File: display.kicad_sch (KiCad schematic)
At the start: 1 part, among them U1 AM6254ATCGHAALW

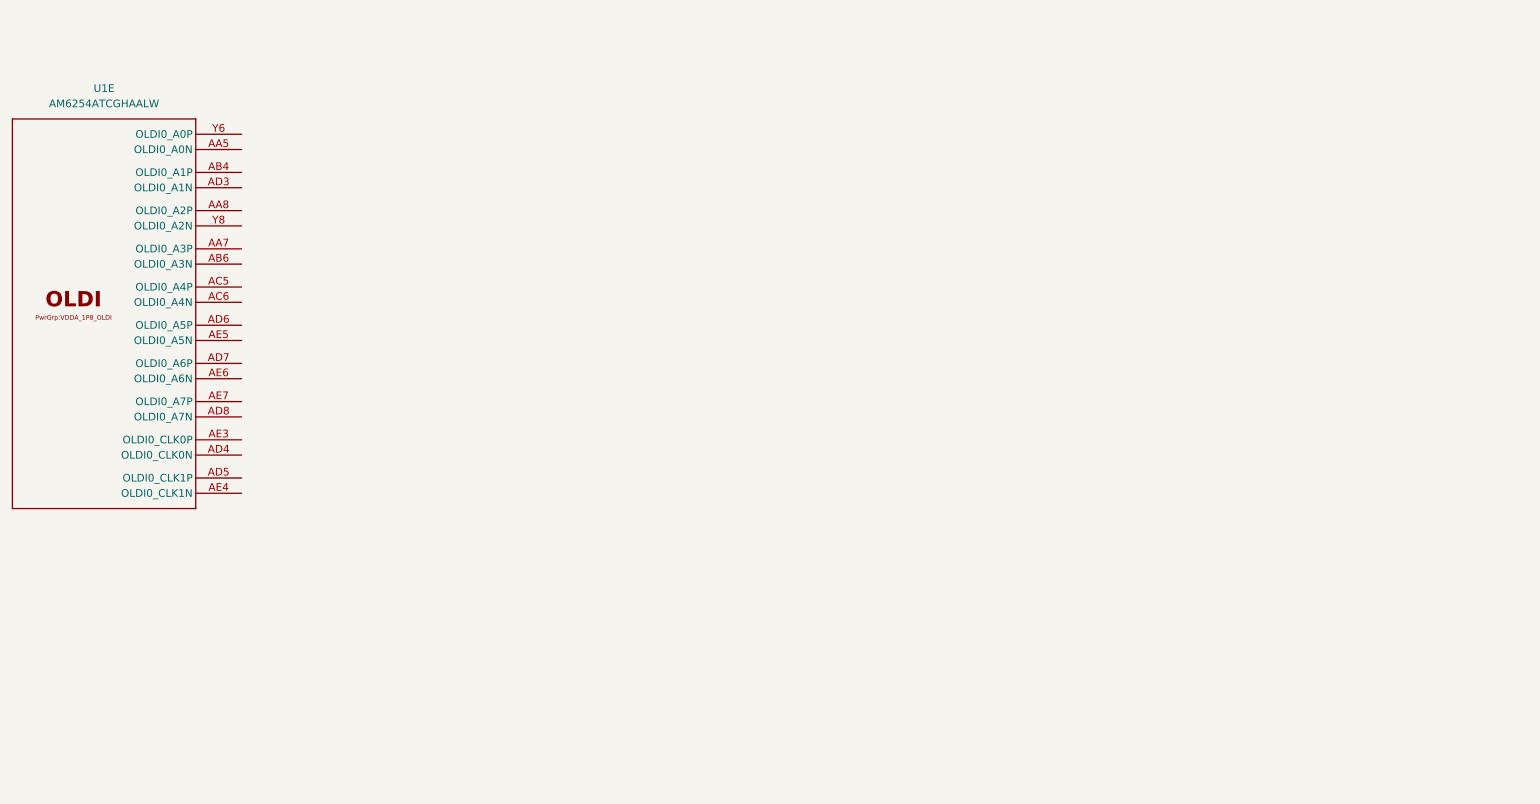
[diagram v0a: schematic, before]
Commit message: Display draft connections
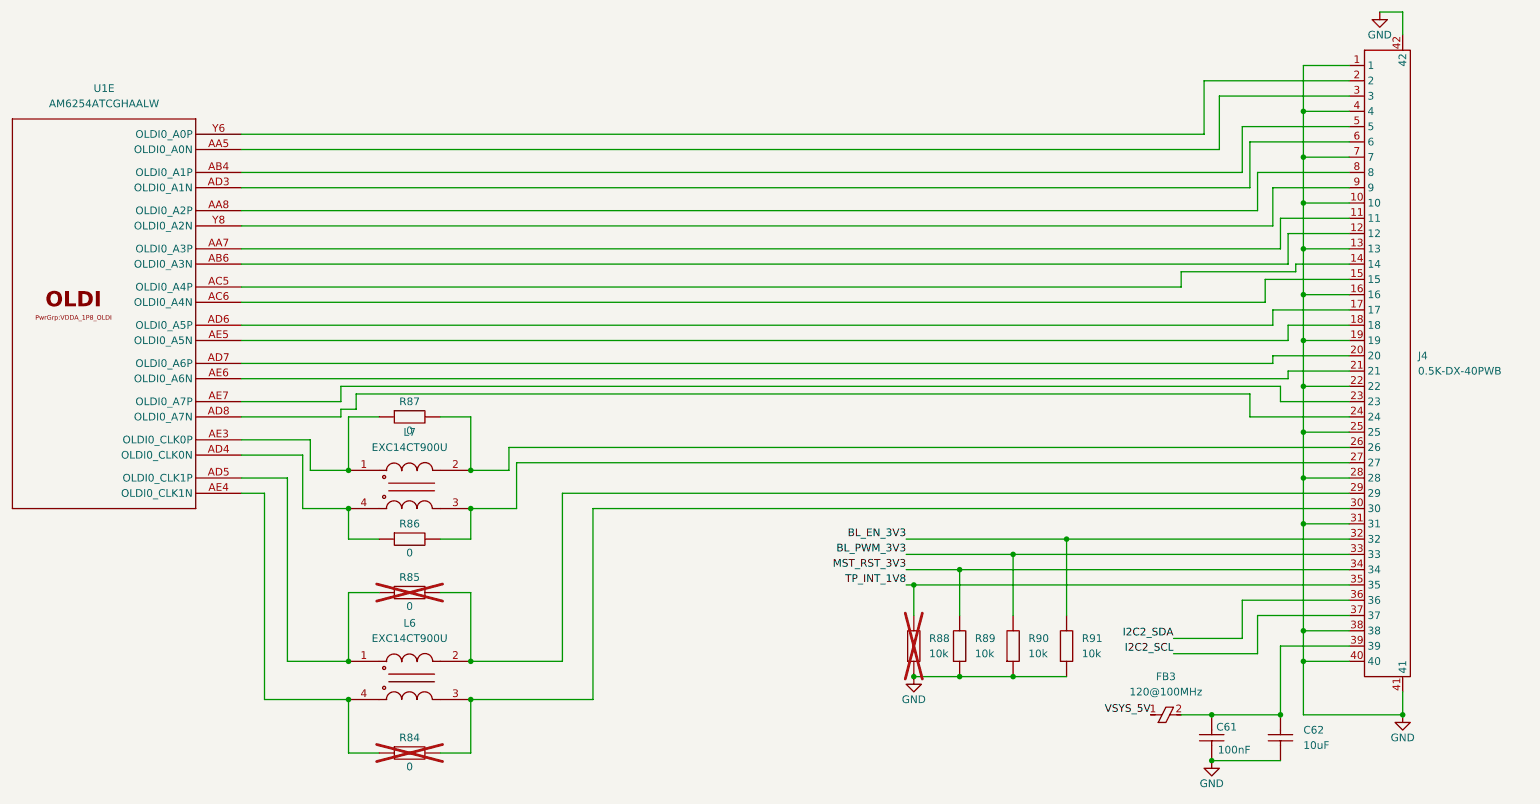
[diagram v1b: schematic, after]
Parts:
- added C61: CC0201KRX5R6BB104, pepy_sym_lib:[CAP_SMD_0201_0603Metric], symbol pepy_sym_lib:[CAP_SMD_0201_0603Metric]YAGEO CC0201KRX5R6BB104
- added C62: CC0402MRX5R5BB106, pepy_sym_lib:[CAP_SMD_0402_1005Metric], symbol pepy_sym_lib:[CAP_SMD_0402_1005Metric]YAGEO CC0402MRX5R5BB106
- added FB3: BLM15PD121SN1D, pepy_sym_lib:[FERRITE_BEAD_0402_1005Metric], symbol pepy_sym_lib:[FERRITE_BEAD_0402_1005Metric]muRata BLM15PD121SN1D
- added J4: 0.5K-DX-40PWB, pepy_sym_lib:[FPC_40P_05MM]HDGC 0.5K-DX-40PWB, symbol pepy_sym_lib:[FPC_40P_05MM]HDGC 0.5K-DX-40PWB
- added L6, L7: EXC14CT900U, pepy_sym_lib:[COMMON_MODE_FILTER]PANASONIC EXC14CT900U, symbol pepy_sym_lib:[COMMON_MODE_FILTER]PANASONIC EXC14CT900U
- added R84, R85, R86, R87: 0402WGF0000TCE, pepy_sym_lib:[RES_SMD_0402_1005Metric], symbol pepy_sym_lib:[RES_SMD_0402_1005Metric]UNI-ROYAL(Uniroyal Elec) 0402WGF0000TCE
- added R88, R89, R90, R91: 0201WMF1002TEE, pepy_sym_lib:[RES_SMD_0201_0603Metric], symbol pepy_sym_lib:[RES_SMD_0201_0603Metric]UNI-ROYAL(Uniroyal Elec) 0201WMF1002TEE
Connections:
- net at U1.AA5 (OLDI0_A0N): now also J4.3
- net at U1.AA7 (OLDI0_A3P): now also J4.11
- net at U1.AA8 (OLDI0_A2P): now also J4.8
- net at U1.AB4 (OLDI0_A1P): now also J4.5
- net at U1.AB6 (OLDI0_A3N): now also J4.12
- net at U1.AC5 (OLDI0_A4P): now also J4.14
- net at U1.AC6 (OLDI0_A4N): now also J4.15
- net at U1.AD3 (OLDI0_A1N): now also J4.6
- net at U1.AD4 (OLDI0_CLK0N): now also L7.4, R86.1
- net at U1.AD5 (OLDI0_CLK1P): now also L6.1, R85.1
- net at U1.AD6 (OLDI0_A5P): now also J4.17
- net at U1.AD7 (OLDI0_A6P): now also J4.20
- net at U1.AD8 (OLDI0_A7N): now also J4.24
- net at U1.AE3 (OLDI0_CLK0P): now also L7.1, R87.1
- net at U1.AE4 (OLDI0_CLK1N): now also L6.4, R84.1
- net at U1.AE5 (OLDI0_A5N): now also J4.18
- net at U1.AE6 (OLDI0_A6N): now also J4.21
- net at U1.AE7 (OLDI0_A7P): now also J4.23
- net at U1.Y6 (OLDI0_A0P): now also J4.2
- net at U1.Y8 (OLDI0_A2N): now also J4.9
- new net: J4.29, L6.2, R85.2
- new net: J4.30, L6.3, R84.2
- new net: C61.2, C62.2, FB3.2, J4.39
- new net: J4.26, L7.2, R87.2
- new net: J4.27, L7.3, R86.2
- new net BL_EN_3V3: J4.32, R91.2
- new net BL_PWM_3V3: J4.33, R90.2
- new net GND: C61.1, C62.1, J4.1, J4.10, J4.13, J4.16, J4.19, J4.22, J4.25, J4.28, J4.31, J4.38, J4.4, J4.40, J4.41, J4.42, J4.7, R88.1, R89.1, R90.1, R91.1
- new net I2C2_SCL: J4.37
- new net I2C2_SDA: J4.36
- new net MST_RST_3V3: J4.34, R89.2
- new net TP_INT_1V8: J4.35, R88.2
- new net VSYS_5V: FB3.1
